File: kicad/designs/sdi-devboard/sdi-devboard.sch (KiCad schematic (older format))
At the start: 48 parts, among them J1 SDI_IP, J2 SDI_IN, J3 CTRL, J4 SDI_O0, J5 SDI_O1, Q1 BSS138, U1 LMH0307

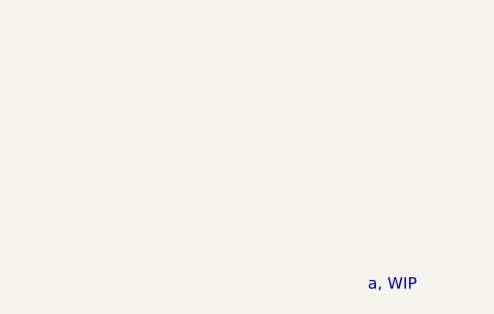
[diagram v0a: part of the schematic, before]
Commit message: Cut revA for sdi-devboard
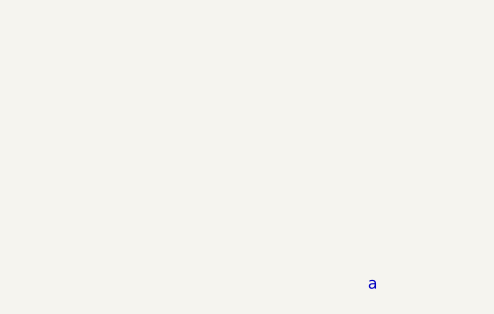
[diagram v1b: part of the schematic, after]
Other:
- note added: "a"
- note removed: "a, WIP"
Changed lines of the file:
@@
 Copyright 2018 Low Latency Consulting, Ltd.\nCC0 1.0 Universal
 Text Notes 10600 7650 0    50   ~ 0
-a, WIP
+a
 Text Notes 8150 7650 0    50   ~ 0
 2018/11/12
